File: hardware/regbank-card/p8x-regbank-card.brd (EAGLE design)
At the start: 160 x 100 mm, 45 parts, among them J1 DIN41612-96M, U1 P0 L0, U10 P2 L1, U11 P2 H0, U12 P2 H1, U13 P3 L0, U14 P3 L1, U15 P3 H0, U16 P3 H1, U17 PTR SEL 0, U18 PTR SEL 1, U19 PTR SEL 2, U2 P0 L1, U20 PTR SEL 3, U21 PTR SEL 4, U22 PTR SEL 5, U23 PTR SEL 6, U24 PTR SEL 7, U25 ADDR LO, U26 ADDR HI, U27 RDBK LO, U28 RDBK HI, U29 RDBK OUT, U3 P0 H0, U30 DLD DEC, U31 DOE DEC, U32 LOAD DEC, U33 SEL+CNT DEC, U34 74HCT02, U35 74HCT14, U36 ZERO P0, U37 74HCT08, U38 74HCT08, U4 P0 H1, U5 P1 L0, U6 P1 L1, U7 P1 H0, U8 P1 H1, U9 P2 L0

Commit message: hw(rev B): reg-bank — 3-bit PSEL decode + PT scratch pointer
Phase 2, step 3. Select decode U33 becomes a 74138 (3-bit PSEL -> -SEL0..4,
so PSEL=4 no longer aliases to P0); count decode moves to a new 74139
(U39, P0-P3 only). U40 (74HCT32) gates the P0-P3 load decoder off when
PSEL2=1 and derives the PT load strobes (-LDL4 = -LDL|-SEL4, etc.). PT
itself is two 74377 latches (U41/U42) loaded from D0-7, driven onto the
pointer bus by two 74244 buffers (U43/U44) when -SEL4 — so it reaches the
address bus and readback path like any pointer. Card retitled REV B.
Validates clean (pin/pad level; not yet electrically DRC'd).

Co-Authored-By: Claude Opus 4.8 <noreply@anthropic.com>
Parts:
- added U39: CNT DEC, p8x:DIP16
- added U40: 74HCT32, p8x:DIP14
- added U41: PT LO, p8x:DIP20
- added U42: PT HI, p8x:DIP20
- added U43: PT SEL LO, p8x:DIP20
- added U44: PT SEL HI, p8x:DIP20
- U33: value SEL+CNT DEC -> SEL DEC
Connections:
- new net -LDH4: U40.11, U42.1
- new net -LDHG: U32.15, U40.6
- new net -LDL4: U40.8, U41.1
- new net -LDLG: U32.1, U40.3
- new net -SEL4: U33.11, U40.10, U40.13, U43.1, U43.19, U44.1, U44.19
- new net PSEL2: J1.C27, U33.3, U40.2, U40.5
- new net PTQ0_0: U41.2, U43.2
- new net PTQ0_1: U41.5, U43.4
- new net PTQ0_2: U41.6, U43.6
- new net PTQ0_3: U41.9, U43.8
- new net PTQ0_4: U41.12, U43.11
- new net PTQ0_5: U41.15, U43.13
- new net PTQ0_6: U41.16, U43.15
- new net PTQ0_7: U41.19, U43.17
- new net PTQ1_0: U42.2, U44.2
- new net PTQ1_1: U42.5, U44.4
- new net PTQ1_2: U42.6, U44.6
- new net PTQ1_3: U42.9, U44.8
- new net PTQ1_4: U42.12, U44.11
- new net PTQ1_5: U42.15, U44.13
- new net PTQ1_6: U42.16, U44.15
- new net PTQ1_7: U42.19, U44.17
- net -CNT0: now also U39.4; no longer U33.12
- net -CNT1: now also U39.5; no longer U33.11
- net -CNT2: now also U39.6; no longer U33.10
- net -CNT3: now also U39.7; no longer U33.9
- net -LDH: now also U40.12, U40.4; no longer U32.15
- net -LDL: now also U40.1, U40.9; no longer U32.1
- net -SEL0: now also U33.15; no longer U33.4
- net -SEL1: now also U33.14; no longer U33.5
- net -SEL2: now also U33.13; no longer U33.6
- net -SEL3: now also U33.12; no longer U33.7
- net CLK: now also U41.11, U42.11
- net CNTN: now also U39.1; no longer U33.15
- net D0: now also U41.3, U42.3
- net D1: now also U41.4, U42.4
- net D2: now also U41.7, U42.7
- net D3: now also U41.8, U42.8
- net D4: now also U41.13, U42.13
- net D5: now also U41.14, U42.14
- net D6: now also U41.17, U42.17
- net D7: now also U41.18, U42.18
- net GND: now also U33.4, U33.5, U39.13, U39.14; no longer U33.1
- net PB0: now also U43.18
- net PB1: now also U43.16
- net PB10: now also U44.14
- net PB11: now also U44.12
- net PB12: now also U44.9
- net PB13: now also U44.7
- net PB14: now also U44.5
- net PB15: now also U44.3
- net PB2: now also U43.14
- net PB3: now also U43.12
- net PB4: now also U43.9
- net PB5: now also U43.7
- net PB6: now also U43.5
- net PB7: now also U43.3
- net PB8: now also U44.18
- net PB9: now also U44.16
- net PSEL0: now also U33.1, U39.2; no longer U33.14, U33.2
- net PSEL1: now also U33.2, U39.3; no longer U33.13, U33.3
- net VCC: now also U33.6, U39.15
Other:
- board text added: "P8X REGISTER BANK CARD REV B (P0=PC P3=SP, PT scratch)"
- board text removed: "P8X REGISTER BANK CARD REV A (P0=PC P3=SP)"

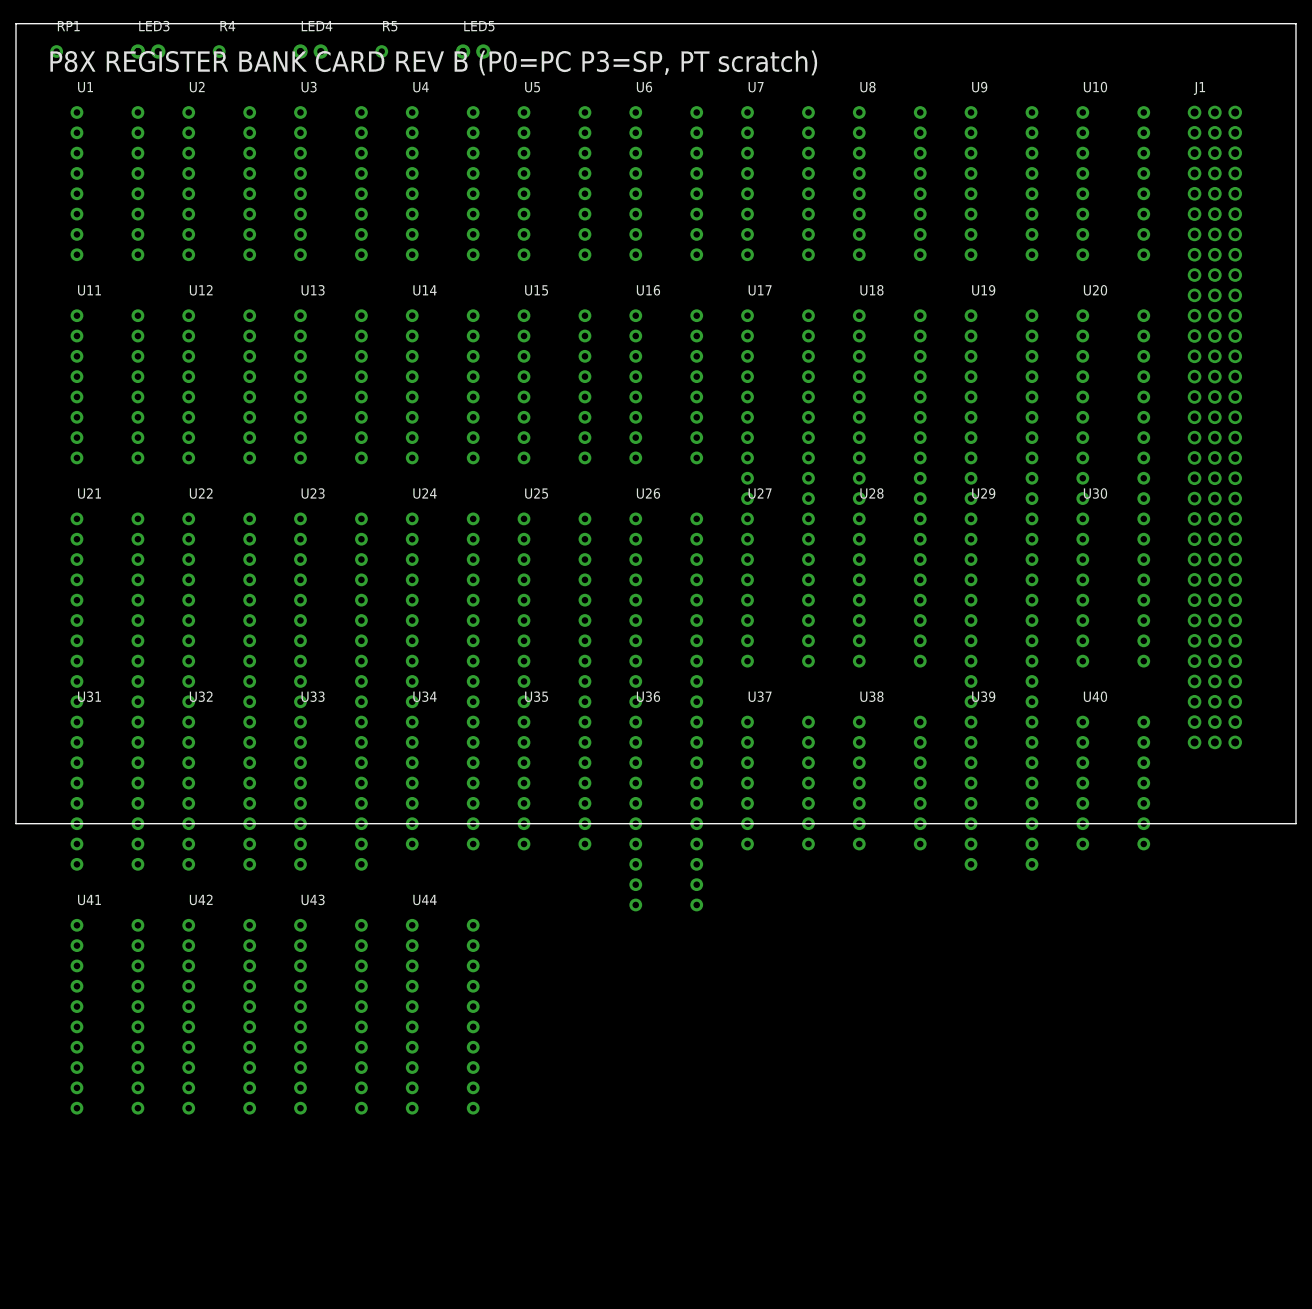
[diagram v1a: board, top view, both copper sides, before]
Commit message: hw: per-IC 100nF decoupling caps on every card
card standards sec.5 requires a decoupling cap per IC; only the backplane had
them. gen_eagle's card() now generates one 100nF cap (CDn, C_DISC footprint)
per IC on the five plug-in cards, placed next to its IC and wired VCC<->GND;
the memory card's separate build does the same for U1-U9.

Caps added: control 18, regbank 44, alu 31, io 15, cf 8, memory 9. All 7
boards regenerate with 0 validation errors; card schematic PDFs refreshed.
Placement is approximate (caps sit just below each IC) pending Fusion routing.

Clears a pre-fab blocker from the backlog.

Co-Authored-By: Claude Opus 4.8 <noreply@anthropic.com>
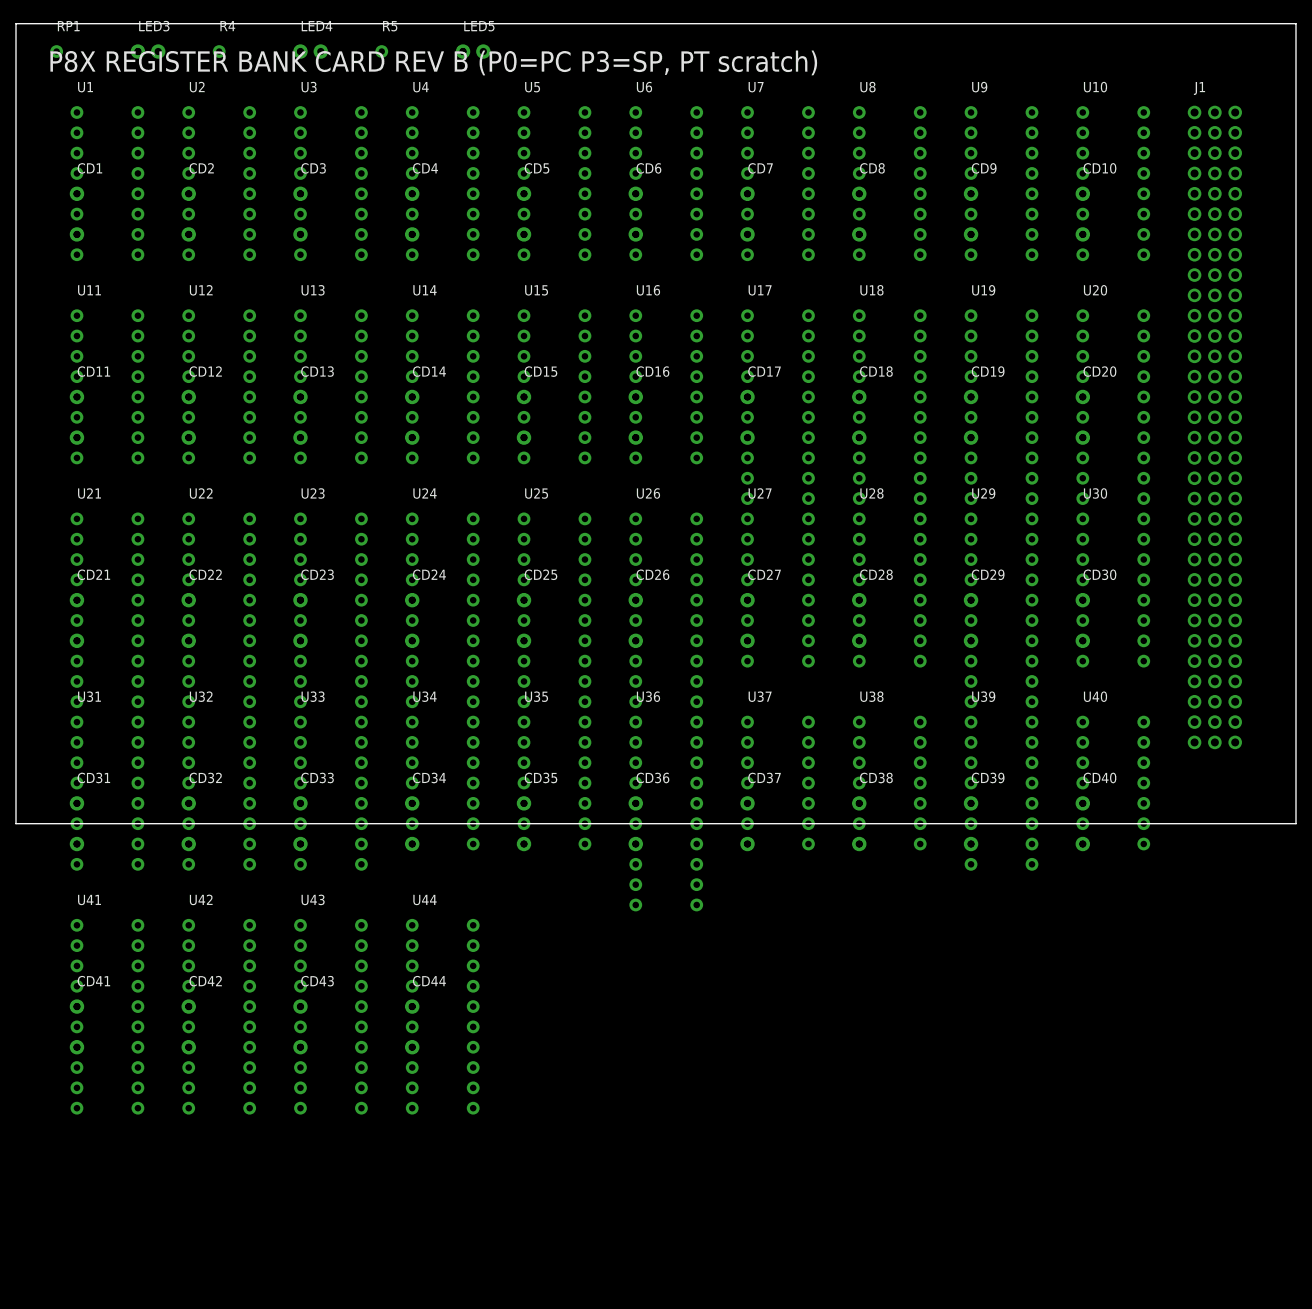
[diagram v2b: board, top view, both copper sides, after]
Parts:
- added CD1, CD10, CD11, CD12, CD13, CD14, CD15, CD16, CD17, CD18, CD19, CD2, CD20, CD21, CD22, CD23, CD24, CD25, CD26, CD27, CD28, CD29, CD3, CD30, CD31, CD32, CD33, CD34, CD35, CD36, CD37, CD38, CD39, CD4, CD40, CD41, CD42, CD43, CD44, CD5, CD6, CD7, CD8, CD9: 100N, p8x:C_DISC
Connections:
- net GND: now also CD1.2, CD10.2, CD11.2, CD12.2, CD13.2, CD14.2, CD15.2, CD16.2, CD17.2, CD18.2, CD19.2, CD2.2, CD20.2, CD21.2, CD22.2, CD23.2, CD24.2, CD25.2, CD26.2, CD27.2, CD28.2, CD29.2, CD3.2, CD30.2, CD31.2, CD32.2, CD33.2, CD34.2, CD35.2, CD36.2, CD37.2, CD38.2, CD39.2, CD4.2, CD40.2, CD41.2, CD42.2, CD43.2, CD44.2, CD5.2, CD6.2, CD7.2, CD8.2, CD9.2
- net VCC: now also CD1.1, CD10.1, CD11.1, CD12.1, CD13.1, CD14.1, CD15.1, CD16.1, CD17.1, CD18.1, CD19.1, CD2.1, CD20.1, CD21.1, CD22.1, CD23.1, CD24.1, CD25.1, CD26.1, CD27.1, CD28.1, CD29.1, CD3.1, CD30.1, CD31.1, CD32.1, CD33.1, CD34.1, CD35.1, CD36.1, CD37.1, CD38.1, CD39.1, CD4.1, CD40.1, CD41.1, CD42.1, CD43.1, CD44.1, CD5.1, CD6.1, CD7.1, CD8.1, CD9.1

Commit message: feat(hw): footprint-aware placement (no component overlaps) + overlap guard
The old auto-placer used a fixed 13.97x25.4mm grid that was tighter than real
footprints — tall DIPs collided with the row below and per-IC caps were buried.

- card(): place by each part's real pad-extent + clearance, flowing in rows that
  wrap at the board width and stack downward (J1 hugs the left edge). Guarantees
  no overlaps. Dense cards (ALU, regbank) now run past the 160x100 outline — they
  genuinely don't fit at safe pitch; arrange by hand when routing (the placement
  PDF flags the overflow).
- memory card: relocate the 9 decoupling caps to a clear bottom strip (they sat
  under the tall DIP-28W ICs).
- validate(): add a rotation-aware footprint-overlap guard (board files) so a
  future card can't silently reintroduce overlaps.
- Regenerated all boards + placement/schematic PDFs.

Verified: 0 overlaps across all 7 boards (rotation-aware); 0 validation errors;
all 6 test suites pass.

Co-Authored-By: Claude Opus 4.8 <noreply@anthropic.com>
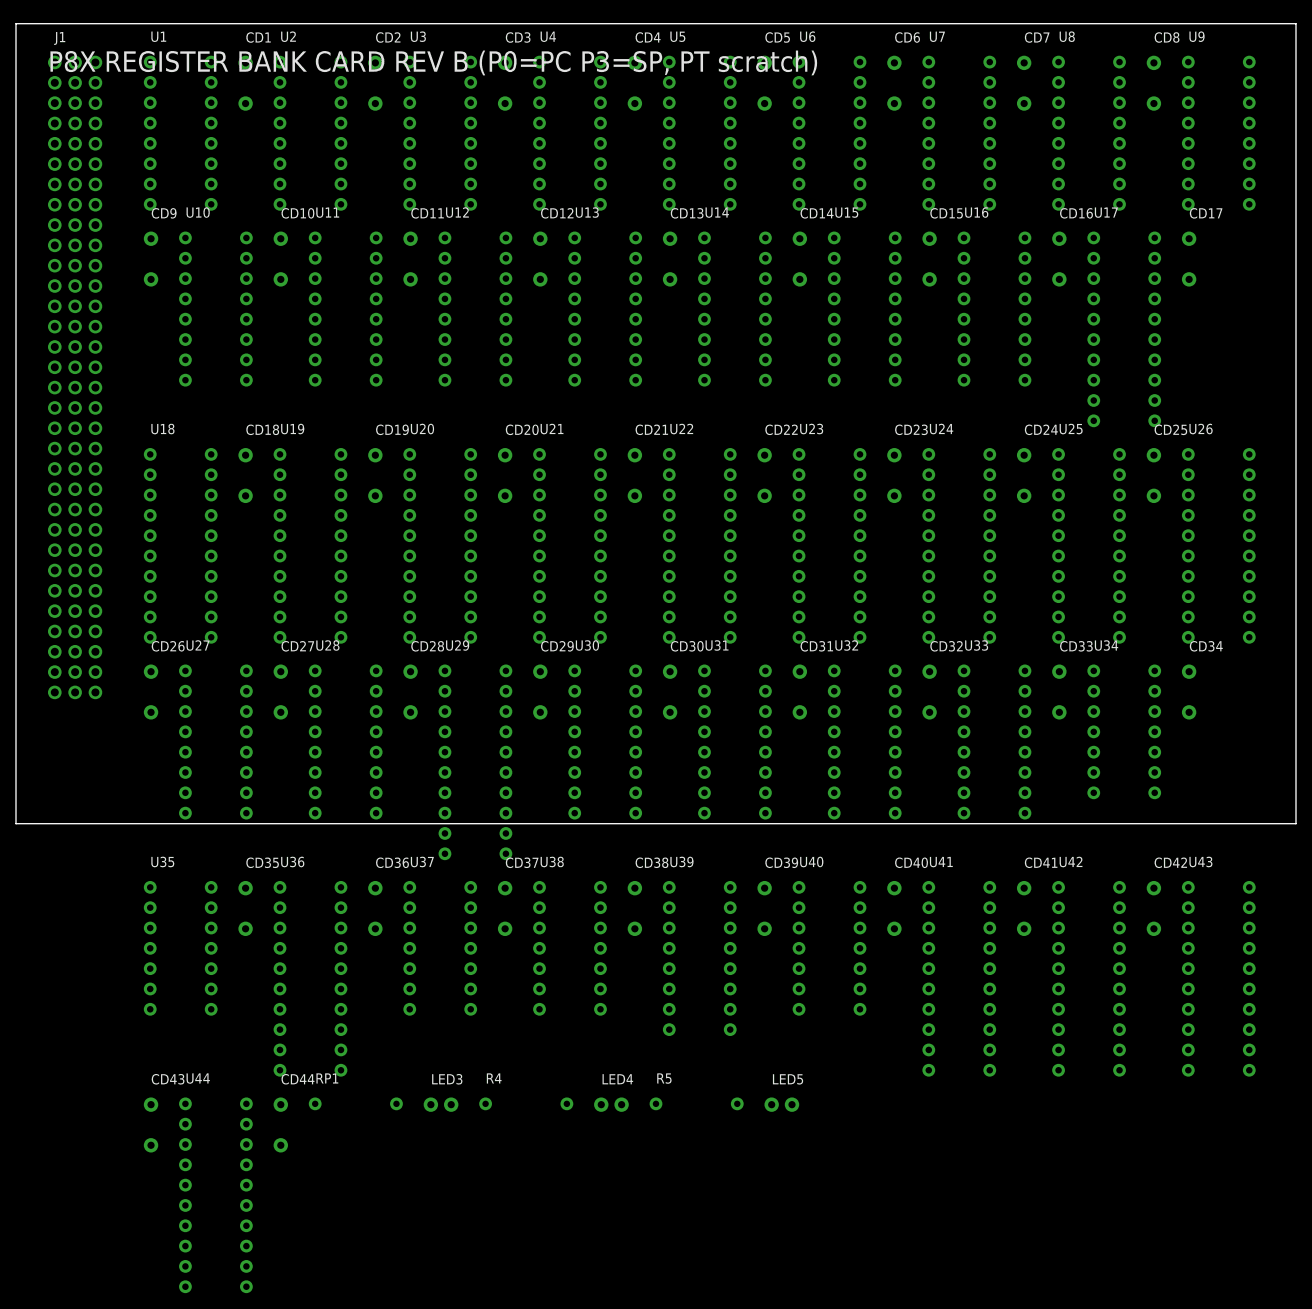
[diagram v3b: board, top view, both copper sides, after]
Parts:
- moved J1 142.6 mm to (4.85, 95.2)
- moved LED5 137.2 mm to (94.5, -35.1)
- moved LED4 136.9 mm to (73.2, -35.1)
- moved LED3 136.6 mm to (51.9, -35.1)
- moved R5 135.9 mm to (80.0, -35.0)
- moved R4 135.7 mm to (58.7, -35.0)
- moved RP1 135.5 mm to (37.4, -35.0)
- moved CD42 121.6 mm to (142.2, -8.06)
- moved CD41 119.3 mm to (126.0, -8.06)
- moved U10 113.3 mm to (21.2, 73.2)
- moved U43 111.1 mm to (146.5, -7.96)
- moved U42 108.8 mm to (130.3, -7.96)
- moved U41 106.6 mm to (114.1, -7.96)
- moved CD9 102.7 mm to (16.9, 73.1)
- moved CD10 100.4 mm to (33.1, 73.1)
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
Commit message: fix(bom): card DIN connectors were undercounted (1 -> 6); label them FABC96R
Two fixes:
- card() built CARDS[name] from `allp`, which omitted J1 — so the 5 plug-in
  cards' DIN41612 edge connectors never reached the BOM (it showed qty 1, only
  the memory card's J1). Include J1 in allp (the schematic renderer already
  filters J1 by name, so rendering is unchanged). BOM now correctly shows 6 card
  connectors + 10 backplane receptacles.
- Card edge connector is FABC96R (user-specified): set the value label on every
  card J1 and name it in the BOM; backplane receptacles noted as the mating part.

Regenerated all boards + PDFs + BOM; all 6 test suites pass.

Co-Authored-By: Claude Opus 4.8 <noreply@anthropic.com>
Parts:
- J1: value DIN41612-96M -> FABC96R
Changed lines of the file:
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@@
 <designrules name="default"><param name="layerSetup" value="(1*2*15*16)"/></designrules>
 <elements>
-<element name="J1" library="p8x" package="DIN96" value="DIN41612-96M" x="4.85" y="95.15"/>
+<element name="J1" library="p8x" package="DIN96" value="FABC96R" x="4.85" y="95.15"/>
 <element name="U1" library="p8x" package="DIP16" value="P0 L0" x="16.78" y="95.20"/>
 <element name="CD1" library="p8x" package="C_DISC" value="100N" x="28.70" y="95.10"/>
